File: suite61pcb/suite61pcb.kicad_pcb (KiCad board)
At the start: 2 copper layers, 176.5 x 111.1 mm, 102 parts, among them J1 Battery JST, J2 FFC_Receiver, J3 FFC_Receiver, SW1 MX_SW_HS, SW10 MX_SW_HS, SW11 MX_SW_HS, SW12 MX_SW_HS, SW13 MX_SW, SW14 MX_SW, SW15 MX_SW_HS, SW16 MX_SW_HS, SW17 MX_SW_HS, SW18 MX_SW_HS, SW19 MX_SW_HS, SW2 MX_SW_HS, SW20 Reset_Button, SW21 MX_SW, SW22 MX_SW, SW23 MX_SW_HS, SW24 MX_SW_HS, SW25 MX_SW_HS, SW26 MX_SW_HS, SW27 MX_SW_HS, SW28 MX_SW_HS, SW29 MX_SW_HS, SW3 MX_SW_HS, SW30 MX_SW_HS, SW31 MX_SW_HS, SW32 MX_SW_HS, SW33 MX_SW_HS, SW34 MX_SW_HS, SW35 MX_SW_HS, SW36 MX_SW_HS, SW37 RotaryEncoder_Switch, SW4 MX_SW_HS, SW5 MX_SW_HS, SW6 MX_SW_HS, SW7 MX_SW_HS, SW8 MX_SW_HS, SW9 MX_SW_HS, U1 nice_nano

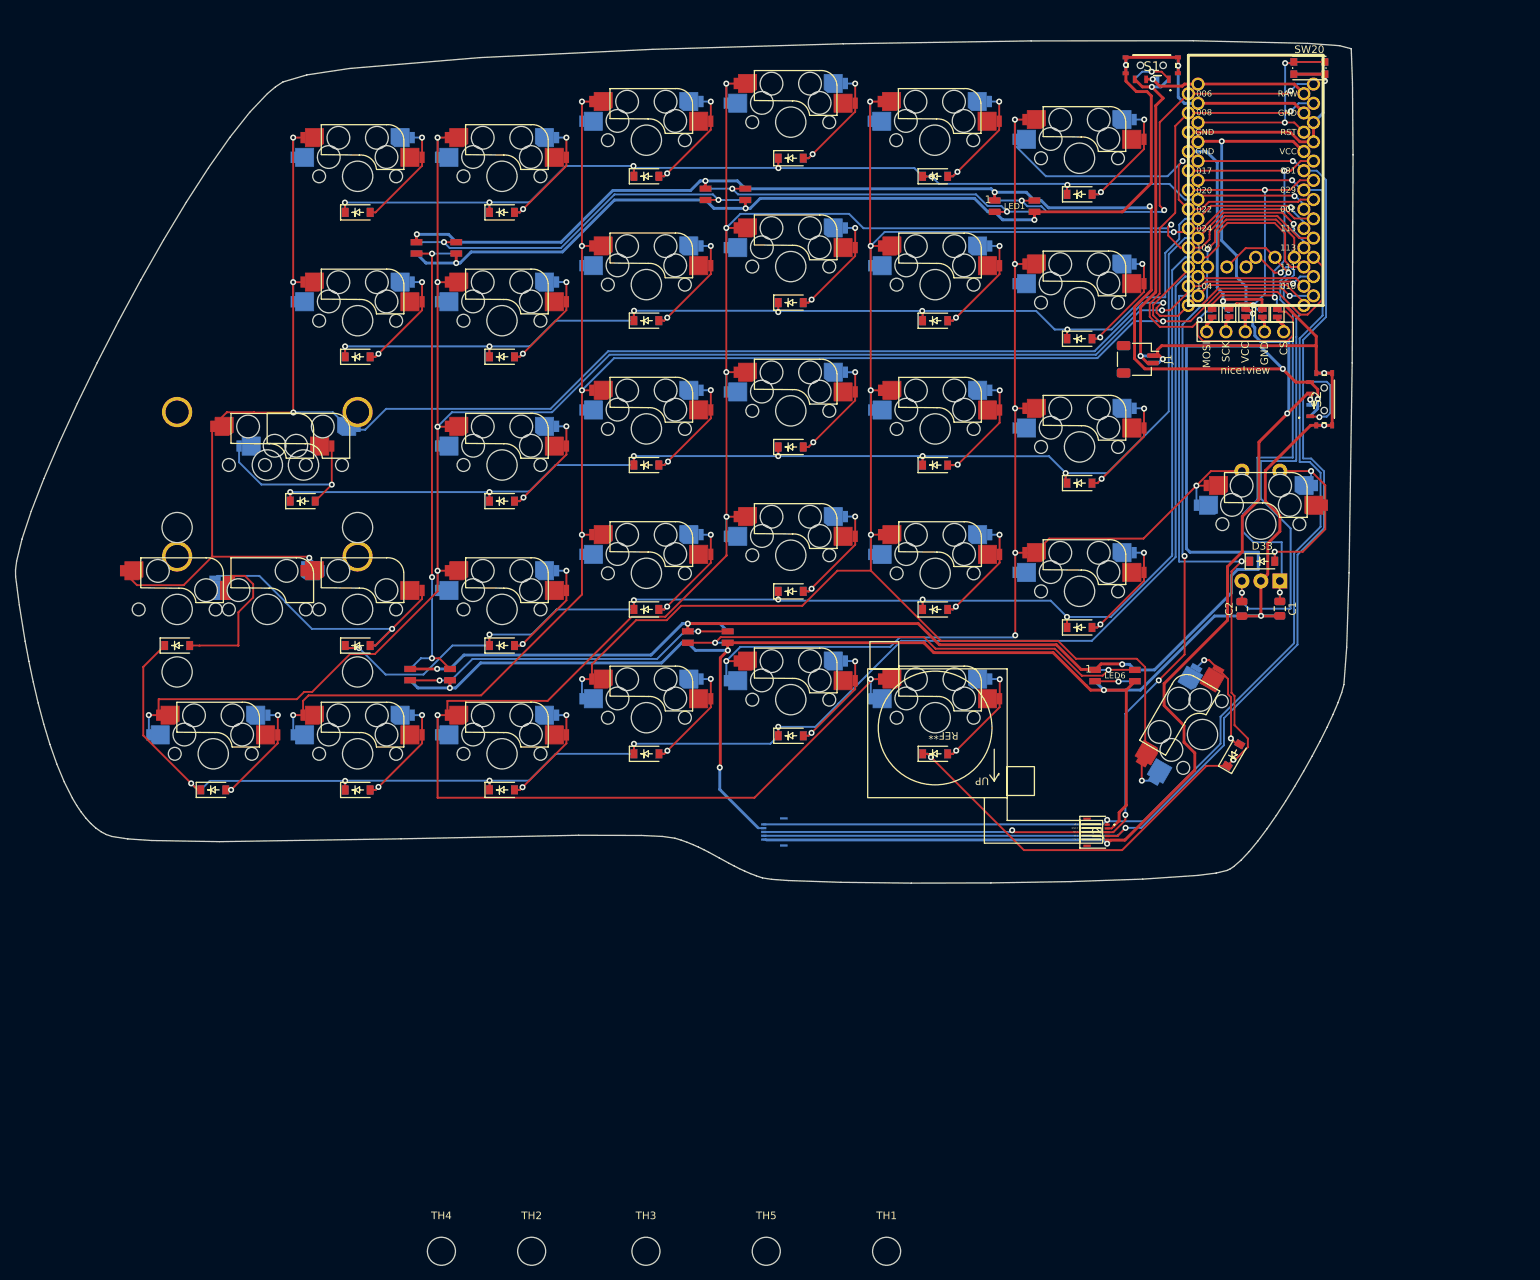
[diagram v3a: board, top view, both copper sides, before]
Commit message: update pcb w logo
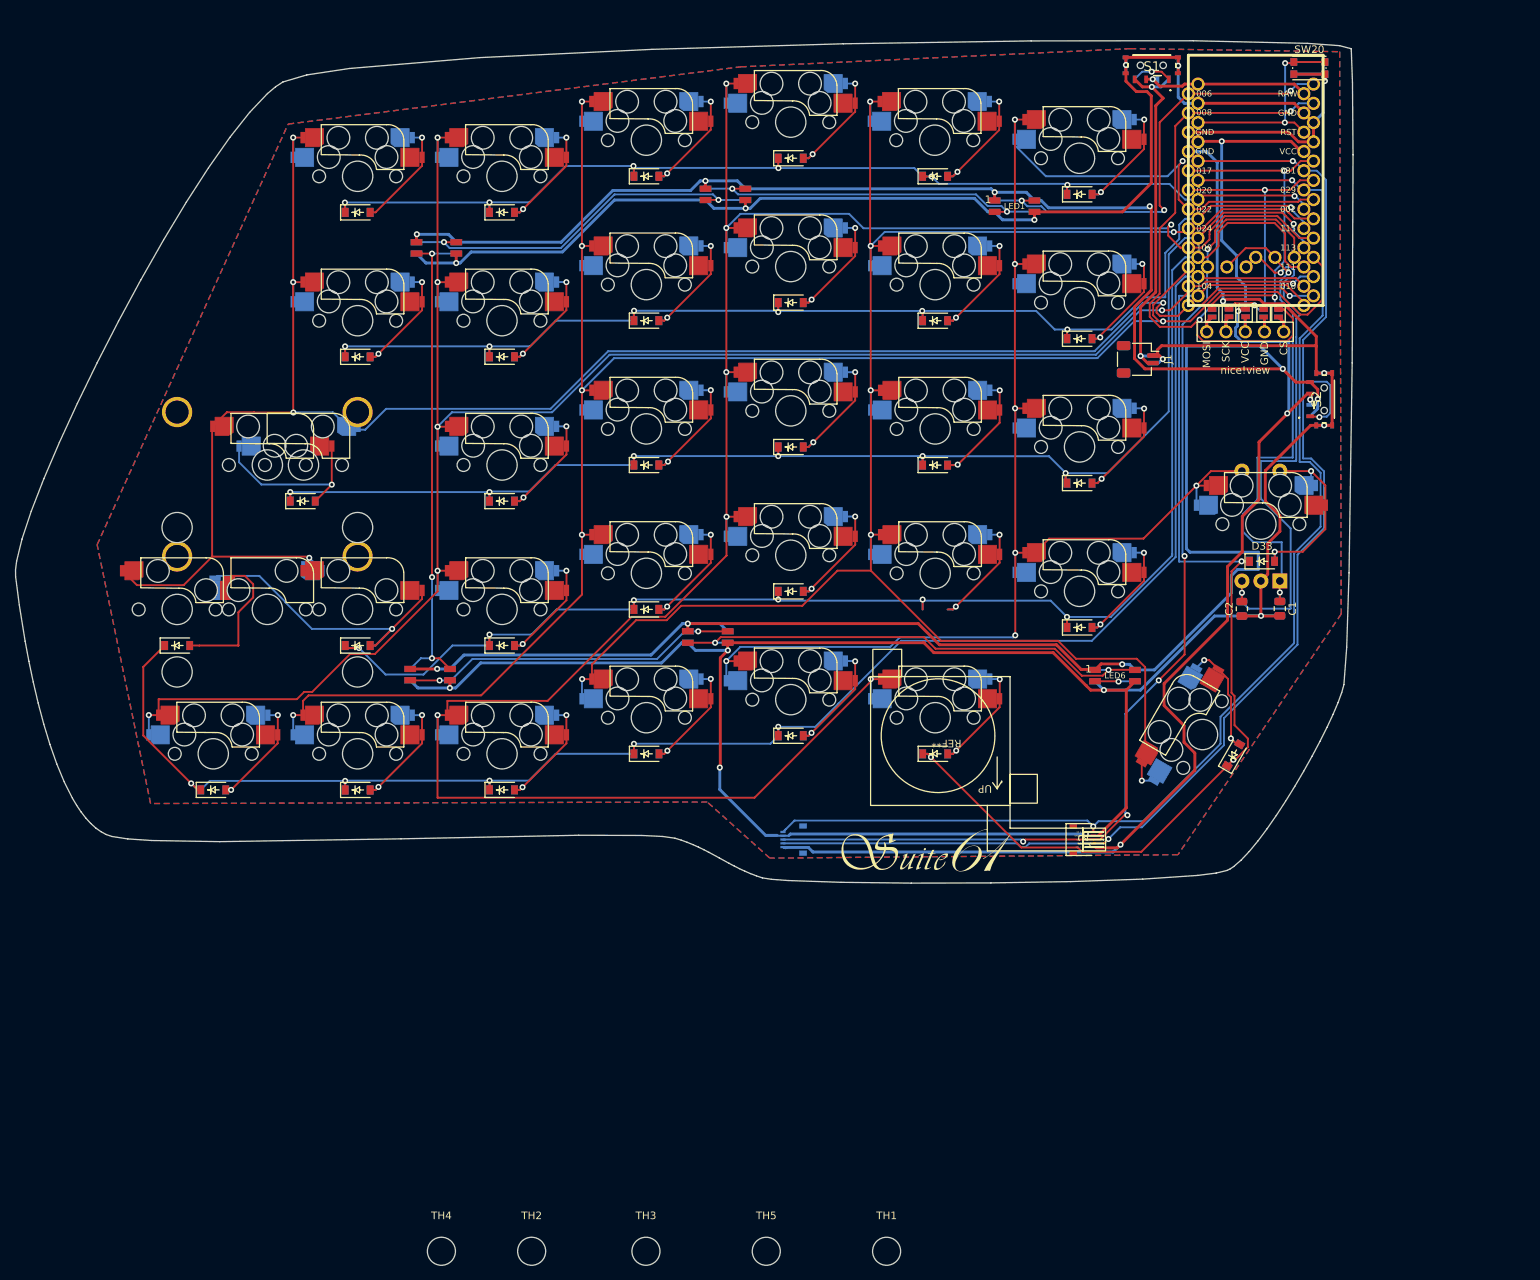
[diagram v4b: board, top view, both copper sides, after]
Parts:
- removed D23: 1N4148W, suite61:D_SOD-123
- moved J3 2.73 mm to (127.6, 130.6)
- moved J2 2.07 mm to (165.4, 130.6)
- moved REF** 1.09 mm to (137.2, 115.1)
- moved REF** 1.09 mm to (155.8, 115.1)
- moved JP2 0.18 mm to (188.6, 62.3)
- moved JP7 0.18 mm to (190.3, 62.3)
- moved JP6 0.16 mm to (192.3, 62.3)
- moved JP1 0.16 mm to (190.5, 62.3)
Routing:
- net GND: track 503.4 -> 550.1 mm, vias 15 -> 16
- net VCC: track 181.4 -> 184.5 mm
- net JSY: track 169.5 -> 167.2 mm
- net JSBTN: track 146.5 -> 144.3 mm
- net JSX: track 164.0 -> 162.5 mm
- net Net-(Display1-Pad5): track 4.00 -> 5.27 mm
- net SDA: track 46.3 -> 45.6 mm
- net Net-(Display1-Pad3): track 3.39 -> 4.01 mm
- net Net-(Display1-Pad2): track 3.70 -> 4.31 mm
- net Net-(Display1-Pad1): track 3.88 -> 4.50 mm
- added copper zone on B.Cu, net GND
- added copper zone on F.Cu, net GND

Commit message: create gerbers
pcb in production from jlcpcb!!!
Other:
- board text added: "battery: 100x80x1.5 1200mAh Filament from UpgradeKeyboards.com"
- board text removed: "battery: 123x43x1.5"
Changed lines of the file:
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@@
     (grid_origin 197.64 50.77)
     (pcbplotparams
-      (layerselection 0x00010fc_ffffffff)
+      (layerselection 0x00010f0_ffffffff)
       (disableapertmacros false)
       (usegerberextensions false)
@@
       (outputformat 1)
       (mirror false)
-      (drillshape 1)
+      (drillshape 0)
       (scaleselection 1)
-      (outputdirectory "")
+      (outputdirectory "gerbers/")
     )
   )
@@
     (fp_arc (start -15.28125 -5.499999) (mid -15.134803 -5.853552) (end -14.78125 -5.999999) (layer "Eco2.User") (width 0.05))
     (fp_arc (start -8.53125 7.500001) (mid -8.677697 7.853554) (end -9.03125 8.000001) (layer "Eco2.User") (width 0.05))
-    (fp_arc (start 15.28125 7.500001) (mid 15.1348 7.853536) (end 14.78125 8.000001) (layer "Eco2.User") (width 0.05))
+    (fp_arc (start 15.28125 7.500001) (mid 15.134806 7.853571) (end 14.78125 8.000001) (layer "Eco2.User") (width 0.05))
     (fp_arc (start -9.03125 -5.999999) (mid -8.677697 -5.853552) (end -8.53125 -5.499999) (layer "Eco2.User") (width 0.05))
     (fp_arc (start 8.53125 -5.499999) (mid 8.677685 -5.853565) (end 9.03125 -5.999999) (layer "Eco2.User") (width 0.05))
-    (fp_arc (start 14.780039 -5.999999) (mid 15.133602 -5.853545) (end 15.280039 -5.499999) (layer "Eco2.User") (width 0.05))
+    (fp_arc (start 14.780039 -5.999999) (mid 15.133567 -5.853539) (end 15.280039 -5.499999) (layer "Eco2.User") (width 0.05))
     (fp_arc (start -14.78125 8.000001) (mid -15.134803 7.853554) (end -15.28125 7.500001) (layer "Eco2.User") (width 0.05))
-    (fp_arc (start 9.03125 8.000001) (mid 8.677693 7.853543) (end 8.53125 7.500001) (layer "Eco2.User") (width 0.05))
+    (fp_arc (start 9.03125 8.000001) (mid 8.677729 7.853537) (end 8.53125 7.500001) (layer "Eco2.User") (width 0.05))
     (pad "" np_thru_hole circle (at 0 0 90) (size 4 4) (drill 4) (layers *.Cu *.Mask))
     (pad "" np_thru_hole circle (at -5.08 0) (size 1.7 1.7) (drill 1.7) (layers *.Cu *.Mask))
@@
     (fp_line (start -15.28125 5.499999) (end -15.28125 -7.500001) (layer "Eco2.User") (width 0.05))
     (fp_line (start -7 -7) (end -7 7) (layer "Eco2.User") (width 0.15))
-    (fp_arc (start 9.03125 5.999999) (mid 8.677694 5.853541) (end 8.53125 5.499999) (layer "Eco2.User") (width 0.05))
+    (fp_arc (start 9.03125 5.999999) (mid 8.677729 5.853535) (end 8.53125 5.499999) (layer "Eco2.User") (width 0.05))
     (fp_arc (start 8.53125 -7.500001) (mid 8.677688 -7.853563) (end 9.03125 -8.000001) (layer "Eco2.User") (width 0.05))
-    (fp_arc (start 14.78125 -8.000001) (mid 15.134807 -7.853543) (end 15.28125 -7.500001) (layer "Eco2.User") (width 0.05))
+    (fp_arc (start 14.78125 -8.000001) (mid 15.134771 -7.853537) (end 15.28125 -7.500001) (layer "Eco2.User") (width 0.05))
     (fp_arc (start -15.28125 -7.500001) (mid -15.134803 -7.853554) (end -14.78125 -8.000001) (layer "Eco2.User") (width 0.05))
     (fp_arc (start -9.03125 -8.000001) (mid -8.677697 -7.853554) (end -8.53125 -7.500001) (layer "Eco2.User") (width 0.05))
@@
       (xy 144.623845 132.402728)
     ) (layer "F.SilkS") (width 0) (fill solid))
-  (gr_rect (start 174.44625 100.32) (end 50.73375 56.6075) (layer "Dwgs.User") (width 0.15) (fill none))
+  (gr_rect (start 167.14 120.42) (end 65.94 39.37) (layer "Dwgs.User") (width 0.15) (fill none))
   (gr_rect (start 175.54 34.02) (end 200.64 79.42) (layer "Dwgs.User") (width 0.15) (fill none))
   (gr_poly
@@
     (effects (font (size 1 1) (thickness 0.15)))
   )
-  (gr_text "battery: 123x43x1.5\n" (at 49.69 64.57 90) (layer "Dwgs.User")
+  (gr_text "battery: 100x80x1.5 1200mAh Filament \nfrom UpgradeKeyboards.com\n" (at 49.69 64.57 90) (layer "Dwgs.User")
     (effects (font (size 1 1) (thickness 0.15)))
   )
